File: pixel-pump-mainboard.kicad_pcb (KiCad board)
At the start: 4 copper layers, 77.4 x 68.3 mm, 134 parts, among them J1 JST NC Valve, J10 BM10B-SRSS-TB(LF)(SN), J11 UART/SWD DNP, J12 TYPE-C-31-M-12, J2 JST NO Valve, J3 6P4C, J4 JST 3 Way Valve, J5 Jack-DC 12V, J6 Power Sw, J7 EXP1, J8 EXP2, J9 BM04B-SRSS-TBT(LF)(SN), Q1 BSS138, Q2 BSS138, Q3 BSS138, Q4 STN4NF20L, Q5 BSS138, SW1 BOOTSEL, U1 LD1117S33TR, U2 TPS62112RSAR, U3 W25Q128JVPIQ, U4 RP2040, Y1 ABMM2-12.000MHZ-E2-T

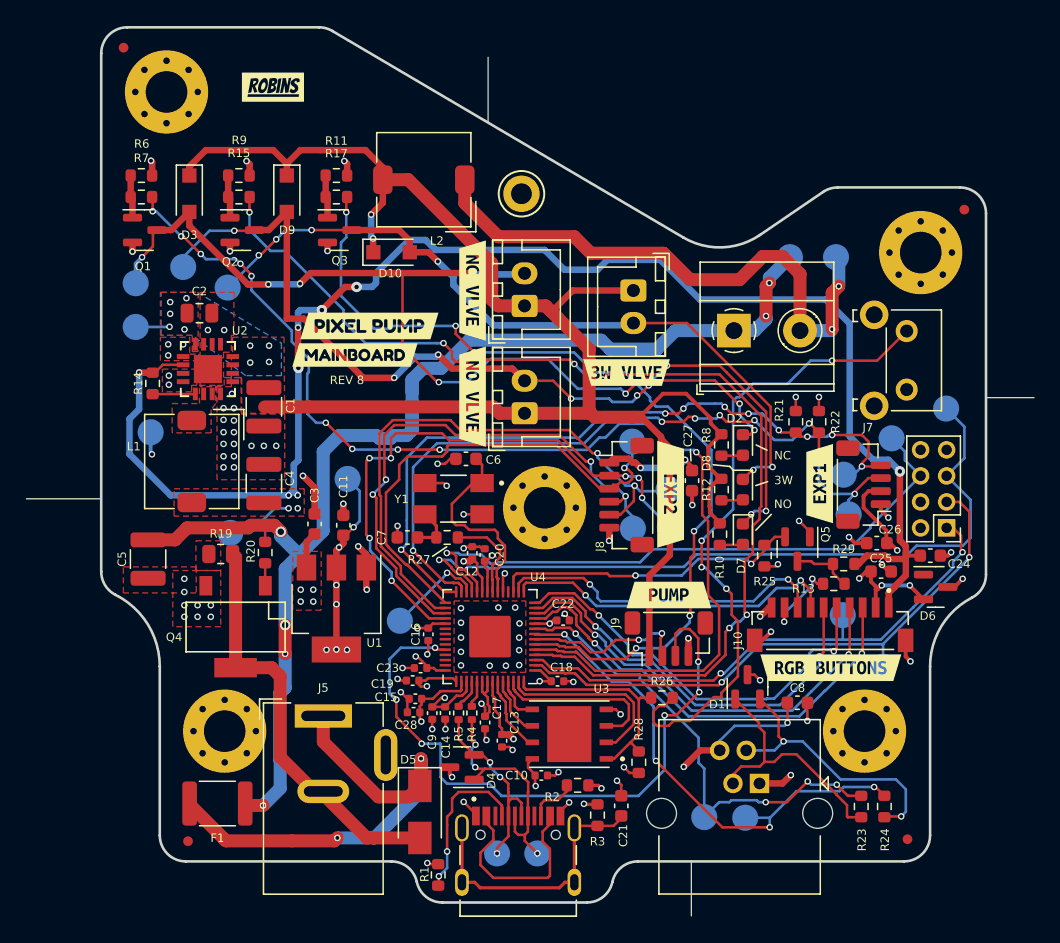
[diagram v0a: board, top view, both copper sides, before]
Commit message: Remove Aisler Outline markers
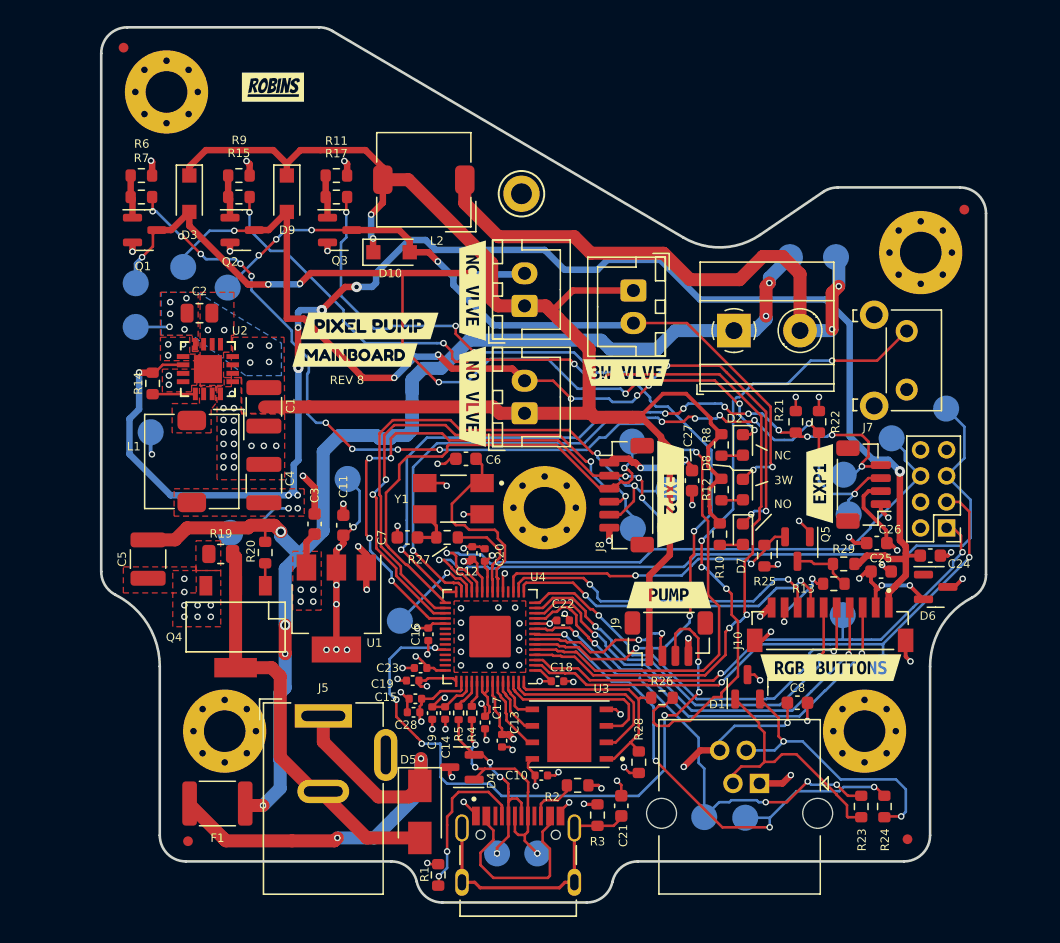
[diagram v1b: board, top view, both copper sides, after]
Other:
- board size 77.4 x 68.3 mm -> 68 x 67.3 mm
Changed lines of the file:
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@@
   (gr_line (start 92.210564 157.59322) (end 103.329656 157.59322) (layer "Edge.Cuts") (width 0.2))
   (gr_arc (start 82.739452 90.3336) (mid 83.265052 90.403899) (end 83.753702 90.609855) (layer "Edge.Cuts") (width 0.2))
-  (gr_line (start 60.2488 126.5682) (end 65.9892 126.5682) (layer "Edge.Cuts") (width 0.05588))
   (gr_arc (start 121.475992 102.987506) (mid 122.013008 102.728973) (end 122.602363 102.640167) (layer "Edge.Cuts") (width 0.2))
   (gr_arc (start 72.5 154.434856) (mid 71.085786 153.84907) (end 70.5 152.434856) (layer "Edge.Cuts") (width 0.2))
@@
   (gr_line (start 132 102.640167) (end 122.602363 102.640167) (layer "Edge.Cuts") (width 0.2))
   (gr_arc (start 105.284883 156.014038) (mid 105.983455 154.878958) (end 107.24011 154.434856) (layer "Edge.Cuts") (width 0.2))
-  (gr_line (start 95.7326 97.6376) (end 95.7326 92.6338) (layer "Edge.Cuts") (width 0.05588))
   (gr_line (start 72.5 154.434856) (end 88.30011 154.434856) (layer "Edge.Cuts") (width 0.2))
   (gr_arc (start 134 132.387559) (mid 133.708285 133.427636) (end 132.918238 134.164307) (layer "Edge.Cuts") (width 0.2))
   (gr_arc (start 92.210564 157.59322) (mid 90.953909 157.149118) (end 90.255337 156.014038) (layer "Edge.Cuts") (width 0.2))
   (gr_arc (start 67.104294 133.951376) (mid 66.298322 133.214015) (end 66 132.163161) (layer "Edge.Cuts") (width 0.2))
-  (gr_line (start 111.3536 158.623) (end 111.3536 154.432) (layer "Edge.Cuts") (width 0.05588))
   (gr_line (start 134 132.387558) (end 134 104.640167) (layer "Edge.Cuts") (width 0.2))
   (gr_arc (start 116.62628 106.292828) (mid 113.711299 107.244981) (end 110.739573 106.48831) (layer "Edge.Cuts") (width 0.2))
@@
   (gr_line (start 82.739452 90.333601) (end 68 90.333601) (layer "Edge.Cuts") (width 0.2))
   (gr_line (start 110.739573 106.48831) (end 83.753702 90.609855) (layer "Edge.Cuts") (width 0.2))
-  (gr_line (start 133.985 118.7958) (end 137.6934 118.7958) (layer "Edge.Cuts") (width 0.05588))
   (gr_arc (start 67.104294 133.951375) (mid 69.582658 136.218759) (end 70.5 139.450136) (layer "Edge.Cuts") (width 0.2))
   (gr_arc (start 129.699999 152.434855) (mid 129.114213 153.849069) (end 127.7 154.434856) (layer "Edge.Cuts") (width 0.2))

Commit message: Add KiKit annotations
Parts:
- added T1: Tab, kikit:Tab, F.Cu at (134.7, 115.9)
- added T2: Tab, kikit:Tab, F.Cu at (80.0, 89.5)
- added T3: Tab, kikit:Tab, F.Cu at (114.6, 155.2)
- added T4: Tab, kikit:Tab, F.Cu at (78.6, 155.2)
- added T5: Tab, kikit:Tab, F.Cu at (65.4, 111.0)
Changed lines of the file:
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@@
     )
   )
+  (footprint "kikit:Tab" (layer "F.Cu")
+    (at 114.552 155.2342 90)
+    (descr "A symbol representing annotation for tab placement")
+    (property "Sheetfile" "pixel-pump-mainboard.kicad_sch")
+    (property "Sheetname" "")
+    (property "exclude_from_bom" "")
+    (attr exclude_from_pos_files exclude_from_bom)
+    (fp_text reference "T3" (at 0 -2 90) (layer "F.SilkS") hide
+      (effects (font (size 1 1) (thickness 0.15)))
+    )
+    (fp_text value "Tab" (at -2.75 -1 90) (layer "Dwgs.User")
+      (effects (font (size 1.2 1.2) (thickness 0.2)))
+    )
+    (fp_text user "KIKIT: width: 3mm" (at -5.5 0) (layer "Dwgs.User")
+      (effects (font (size 1 1) (thickness 0.15)))
+    )
+    (fp_line (start 0.25 1) (end 0.25 -1) (layer "Dwgs.User") (width 0.3))
+    (fp_line (start 0.25 0) (end -0.75 -1) (layer "Dwgs.User") (width 0.3))
+    (fp_line (start 0.25 0) (end -0.75 1) (layer "Dwgs.User") (width 0.3))
+    (fp_line (start 0.25 0) (end -2.75 0) (layer "Dwgs.User") (width 0.3))
+  )
   (footprint "STN4NF20L:SOT223" (layer "F.Cu")
     (at 76.327 133.2484 180)
@@
     )
   )
+  (footprint "kikit:Tab" (layer "F.Cu")
+    (at 65.3648 111.0234)
+    (descr "A symbol representing annotation for tab placement")
+    (property "Sheetfile" "pixel-pump-mainboard.kicad_sch")
+    (property "Sheetname" "")
+    (property "exclude_from_bom" "")
+    (attr exclude_from_pos_files exclude_from_bom)
+    (fp_text reference "T5" (at 0 -2) (layer "F.SilkS") hide
+      (effects (font (size 1 1) (thickness 0.15)))
+    )
+    (fp_text value "Tab" (at -2.75 -1) (layer "Dwgs.User")
+      (effects (font (size 1.2 1.2) (thickness 0.2)))
+    )
+    (fp_text user "KIKIT: width: 3mm" (at -5.5 0 90) (layer "Dwgs.User")
+      (effects (font (size 1 1) (thickness 0.15)))
+    )
+    (fp_line (start 0.25 1) (end 0.25 -1) (layer "Dwgs.User") (width 0.3))
+    (fp_line (start 0.25 0) (end -2.75 0) (layer "Dwgs.User") (width 0.3))
+    (fp_line (start 0.25 0) (end -0.75 -1) (layer "Dwgs.User") (width 0.3))
+    (fp_line (start 0.25 0) (end -0.75 1) (layer "Dwgs.User") (width 0.3))
+  )
+  (footprint "kikit:Tab" (layer "F.Cu")
+    (at 134.7216 115.9256 180)
+    (descr "A symbol representing annotation for tab placement")
+    (property "Sheetfile" "pixel-pump-mainboard.kicad_sch")
+    (property "Sheetname" "")
+    (property "exclude_from_bom" "")
+    (attr exclude_from_pos_files exclude_from_bom)
+    (fp_text reference "T1" (at 0 -2) (layer "F.SilkS") hide
+      (effects (font (size 1 1) (thickness 0.15)))
+    )
+    (fp_text value "Tab" (at -2.75 -1) (layer "Dwgs.User")
+      (effects (font (size 1.2 1.2) (thickness 0.2)))
+    )
+    (fp_text user "KIKIT: width: 3mm" (at -5.5 0 90) (layer "Dwgs.User")
+      (effects (font (size 1 1) (thickness 0.15)))
+    )
+    (fp_line (start 0.25 1) (end 0.25 -1) (layer "Dwgs.User") (width 0.3))
+    (fp_line (start 0.25 0) (end -0.75 -1) (layer "Dwgs.User") (width 0.3))
+    (fp_line (start 0.25 0) (end -0.75 1) (layer "Dwgs.User") (width 0.3))
+    (fp_line (start 0.25 0) (end -2.75 0) (layer "Dwgs.User") (width 0.3))
+  )
   (footprint "Resistor_SMD:R_0603_1608Metric" (layer "F.Cu")
     (at 104.14 150.876 90)
@@
     )
   )
+  (footprint "kikit:Tab" (layer "F.Cu")
+    (at 78.611 155.176 90)
+    (descr "A symbol representing annotation for tab placement")
+    (property "Sheetfile" "pixel-pump-mainboard.kicad_sch")
+    (property "Sheetname" "")
+    (property "exclude_from_bom" "")
+    (attr exclude_from_pos_files exclude_from_bom)
+    (fp_text reference "T4" (at 0 -2 90) (layer "F.SilkS") hide
+      (effects (font (size 1 1) (thickness 0.15)))
+    )
+    (fp_text value "Tab" (at -2.75 -1 90) (layer "Dwgs.User")
+      (effects (font (size 1.2 1.2) (thickness 0.2)))
+    )
+    (fp_text user "KIKIT: width: 3mm" (at -5.5 0) (layer "Dwgs.User")
+      (effects (font (size 1 1) (thickness 0.15)))
+    )
+    (fp_line (start 0.25 0) (end -2.75 0) (layer "Dwgs.User") (width 0.3))
+    (fp_line (start 0.25 1) (end 0.25 -1) (layer "Dwgs.User") (width 0.3))
+    (fp_line (start 0.25 0) (end -0.75 1) (layer "Dwgs.User") (width 0.3))
+    (fp_line (start 0.25 0) (end -0.75 -1) (layer "Dwgs.User") (width 0.3))
+  )
   (footprint "kibuzzard-6107E0E1" (layer "F.Cu")
     (at 122.0724 139.5476)
@@
       ) (layer "F.SilkS") (width 0) (fill solid))
   )
+  (footprint "kikit:Tab" (layer "F.Cu")
+    (at 80.0354 89.5022 -90)
+    (descr "A symbol representing annotation for tab placement")
+    (property "Sheetfile" "pixel-pump-mainboard.kicad_sch")
+    (property "Sheetname" "")
+    (property "exclude_from_bom" "")
+    (attr exclude_from_pos_files exclude_from_bom)
+    (fp_text reference "T2" (at 0 -2 90) (layer "F.SilkS") hide
+      (effects (font (size 1 1) (thickness 0.15)))
+    )
+    (fp_text value "Tab" (at -2.75 -1 90) (layer "Dwgs.User")
+      (effects (font (size 1.2 1.2) (thickness 0.2)))
+    )
+    (fp_text user "KIKIT: width: 2.5mm" (at -5.5 0) (layer "Dwgs.User")
+      (effects (font (size 1 1) (thickness 0.15)))
+    )
+    (fp_line (start 0.25 0) (end -0.75 -1) (layer "Dwgs.User") (width 0.3))
+    (fp_line (start 0.25 0) (end -0.75 1) (layer "Dwgs.User") (width 0.3))
+    (fp_line (start 0.25 0) (end -2.75 0) (layer "Dwgs.User") (width 0.3))
+    (fp_line (start 0.25 1) (end 0.25 -1) (layer "Dwgs.User") (width 0.3))
+  )
   (footprint "LED_SMD:LED_0603_1608Metric" (layer "F.Cu")

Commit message: Rev 8 panel settings and export
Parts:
- removed T5: Tab, kikit:Tab
- moved T4 31.7 mm to (65.3, 126.4), turned to 0 degrees
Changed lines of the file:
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@@
       (effects (font (size 1.2 1.2) (thickness 0.2)))
     )
-    (fp_text user "KIKIT: width: 3mm" (at -5.5 0) (layer "Dwgs.User")
+    (fp_text user "KIKIT: width: 2.5mm" (at -5.5 0) (layer "Dwgs.User")
       (effects (font (size 1 1) (thickness 0.15)))
     )
@@
   )
   (footprint "kikit:Tab" (layer "F.Cu")
-    (at 65.3648 111.0234)
-    (descr "A symbol representing annotation for tab placement")
-    (property "Sheetfile" "pixel-pump-mainboard.kicad_sch")
-    (property "Sheetname" "")
-    (property "exclude_from_bom" "")
-    (attr exclude_from_pos_files exclude_from_bom)
-    (fp_text reference "T5" (at 0 -2) (layer "F.SilkS") hide
-      (effects (font (size 1 1) (thickness 0.15)))
-    )
-    (fp_text value "Tab" (at -2.75 -1) (layer "Dwgs.User")
-      (effects (font (size 1.2 1.2) (thickness 0.2)))
-    )
-    (fp_text user "KIKIT: width: 3mm" (at -5.5 0 90) (layer "Dwgs.User")
-      (effects (font (size 1 1) (thickness 0.15)))
-    )
-    (fp_line (start 0.25 1) (end 0.25 -1) (layer "Dwgs.User") (width 0.3))
-    (fp_line (start 0.25 0) (end -2.75 0) (layer "Dwgs.User") (width 0.3))
-    (fp_line (start 0.25 0) (end -0.75 -1) (layer "Dwgs.User") (width 0.3))
-    (fp_line (start 0.25 0) (end -0.75 1) (layer "Dwgs.User") (width 0.3))
-  )
-  (footprint "kikit:Tab" (layer "F.Cu")
     (at 134.7216 115.9256 180)
     (descr "A symbol representing annotation for tab placement")
@@
       (effects (font (size 1.2 1.2) (thickness 0.2)))
     )
-    (fp_text user "KIKIT: width: 3mm" (at -5.5 0 90) (layer "Dwgs.User")
+    (fp_text user "KIKIT: width: 2.5mm" (at -5.5 0 90) (layer "Dwgs.User")
       (effects (font (size 1 1) (thickness 0.15)))
     )
@@
     )
   )
-  (footprint "kikit:Tab" (layer "F.Cu")
-    (at 78.611 155.176 90)
-    (descr "A symbol representing annotation for tab placement")
-    (property "Sheetfile" "pixel-pump-mainboard.kicad_sch")
-    (property "Sheetname" "")
-    (property "exclude_from_bom" "")
-    (attr exclude_from_pos_files exclude_from_bom)
-    (fp_text reference "T4" (at 0 -2 90) (layer "F.SilkS") hide
-      (effects (font (size 1 1) (thickness 0.15)))
-    )
-    (fp_text value "Tab" (at -2.75 -1 90) (layer "Dwgs.User")
-      (effects (font (size 1.2 1.2) (thickness 0.2)))
-    )
-    (fp_text user "KIKIT: width: 3mm" (at -5.5 0) (layer "Dwgs.User")
-      (effects (font (size 1 1) (thickness 0.15)))
-    )
-    (fp_line (start 0.25 0) (end -2.75 0) (layer "Dwgs.User") (width 0.3))
-    (fp_line (start 0.25 1) (end 0.25 -1) (layer "Dwgs.User") (width 0.3))
-    (fp_line (start 0.25 0) (end -0.75 1) (layer "Dwgs.User") (width 0.3))
-    (fp_line (start 0.25 0) (end -0.75 -1) (layer "Dwgs.User") (width 0.3))
-  )
   (footprint "kibuzzard-6107E0E1" (layer "F.Cu")
     (at 122.0724 139.5476)
@@
     )
   )
+  (footprint "kikit:Tab" (layer "F.Cu")
+    (at 65.278 126.365)
+    (descr "A symbol representing annotation for tab placement")
+    (property "Sheetfile" "pixel-pump-mainboard.kicad_sch")
+    (property "Sheetname" "")
+    (property "exclude_from_bom" "")
+    (attr exclude_from_pos_files exclude_from_bom)
+    (fp_text reference "T4" (at 0 -2) (layer "F.SilkS") hide
+      (effects (font (size 1 1) (thickness 0.15)))
+    )
+    (fp_text value "Tab" (at -2.75 -1) (layer "Dwgs.User")
+      (effects (font (size 1.2 1.2) (thickness 0.2)))
+    )
+    (fp_text user "KIKIT: width: 2.5mm" (at -5.5 0 90) (layer "Dwgs.User")
+      (effects (font (size 1 1) (thickness 0.15)))
+    )
+    (fp_line (start 0.25 0) (end -2.75 0) (layer "Dwgs.User") (width 0.3))
+    (fp_line (start 0.25 1) (end 0.25 -1) (layer "Dwgs.User") (width 0.3))
+    (fp_line (start 0.25 0) (end -0.75 1) (layer "Dwgs.User") (width 0.3))
+    (fp_line (start 0.25 0) (end -0.75 -1) (layer "Dwgs.User") (width 0.3))
+  )
   (footprint "TerminalBlock_Phoenix:TerminalBlock_Phoenix_MKDS-1,5-2-5.08_1x02_P5.08mm_Horizontal" (layer "F.Cu")

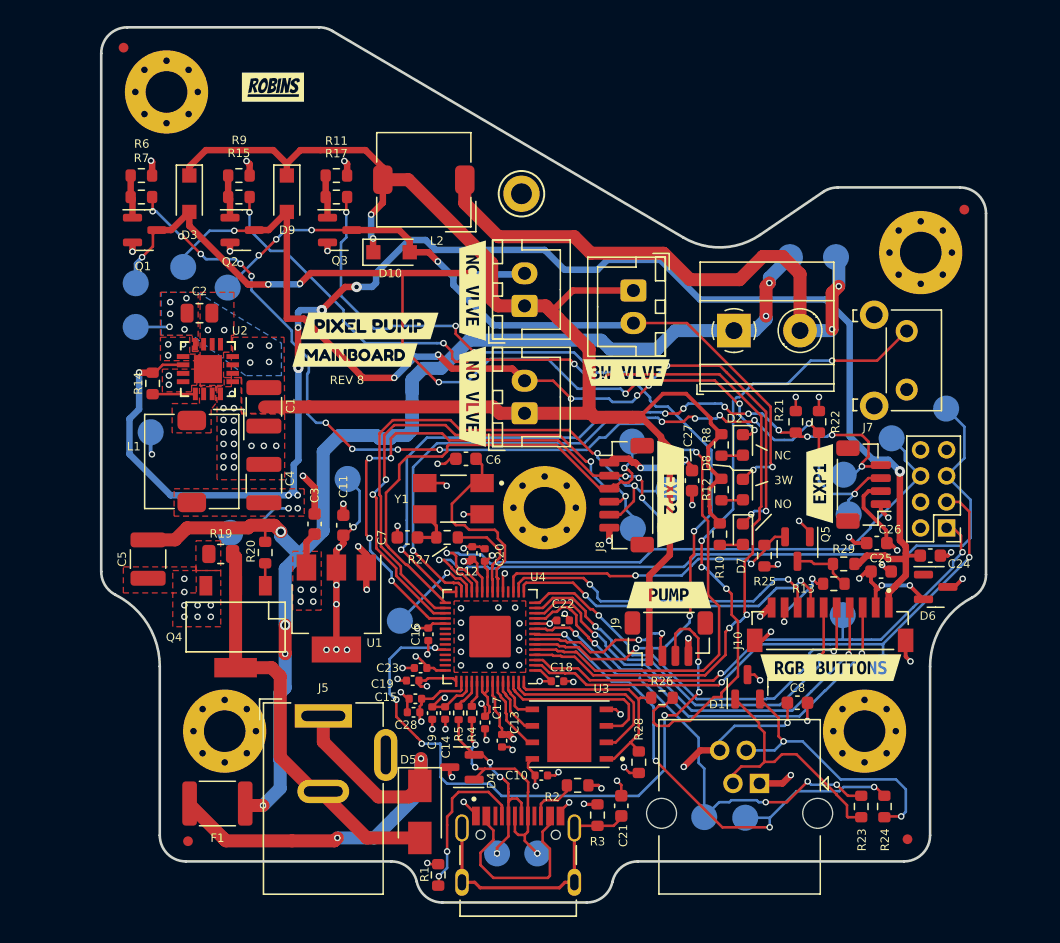
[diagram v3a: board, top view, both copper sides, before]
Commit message: Fixed issues and generated the final pos file
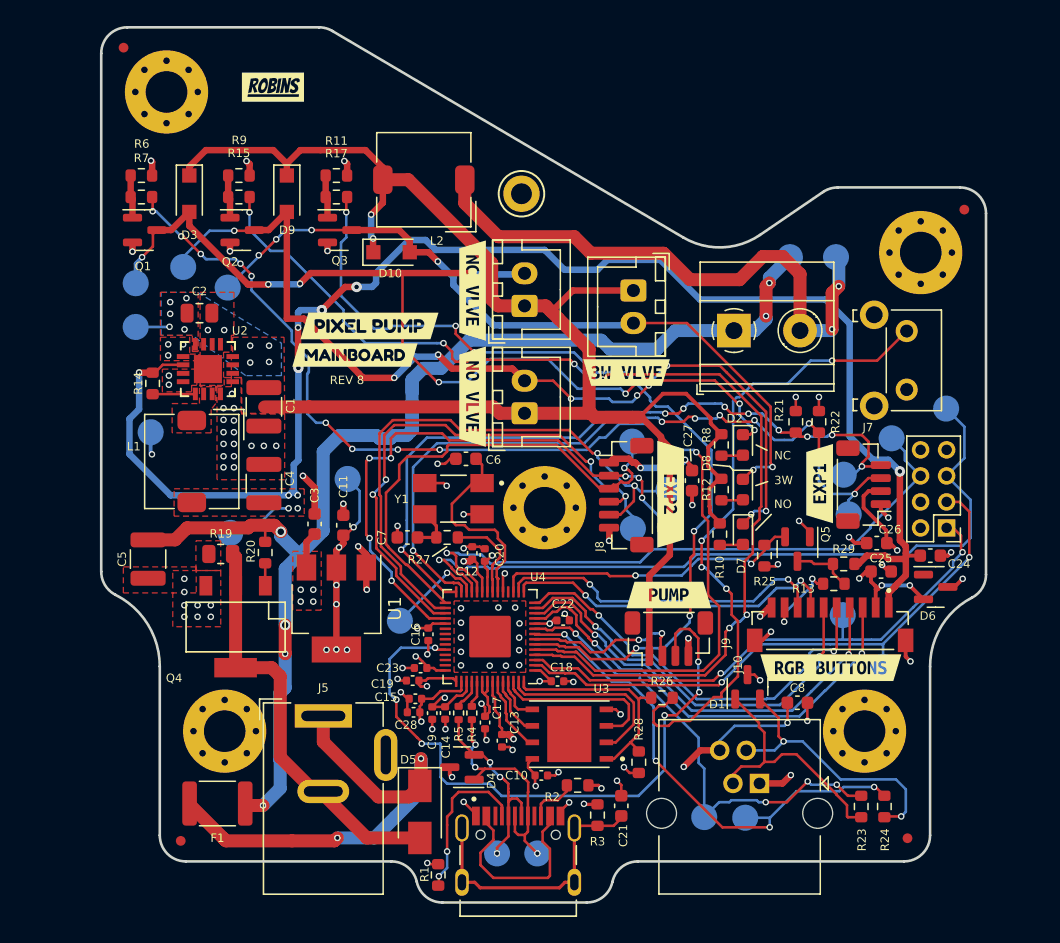
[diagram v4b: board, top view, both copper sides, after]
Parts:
- J7, J9: footprint Connector_JST:JST_SH_BM04B-SRSS-TB_1x04-1MP_P1.00mm_Vertical -> BM04B-SRSS-TBT:BM04B-SRSS-TBT
- J8: footprint Connector_JST:JST_SH_BM06B-SRSS-TB_1x06-1MP_P1.00mm_Vertical -> BM06B-SRSS-TBT:BM06B-SRSS-TBT
- U1: footprint Package_TO_SOT_SMD:SOT-223-3_TabPin2 -> Package_TO_SOT_SMD:SOT-223
- moved FID2 85.6 mm to (128.0, 152.7)
- moved FID1 61.2 mm to (67.7, 91.9)
- moved FID4 55.9 mm to (72.1, 152.9)
- moved Q4 3.15 mm to (76.3, 136.4)
- moved J10 1.83 mm to (122.0, 136.8)
- moved J12 1.07 mm to (98.0, 155.0)
- moved J7 0.46 mm to (124.1, 125.5)
- moved J9 0.46 mm to (109.6, 136.9)
- moved J8 0.43 mm to (106.8, 126.3)

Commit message: Rev 9
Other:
- board text added: "REV 9"
- board text removed: "REV 8"
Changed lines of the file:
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@@
   (gr_arc (start 129.699998 139.450136) (mid 130.567849 136.355905) (end 132.918238 134.164307) (layer "Edge.Cuts") (width 0.2))
   (gr_line (start 70.5 139.450136) (end 70.5 152.434856) (layer "Edge.Cuts") (width 0.2))
-  (gr_text "REV 8" (at 84.8868 117.4496) (layer "F.SilkS")
+  (gr_text "REV 9" (at 84.8868 117.4496) (layer "F.SilkS")
     (effects (font (size 0.65 0.65) (thickness 0.13)))
   )
